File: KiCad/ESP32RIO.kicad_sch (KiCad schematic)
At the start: 40 parts, among them J1 Screw_Terminal_01x08, J2 Screw_Terminal_01x08, J3 Screw_Terminal_01x08, J4 Screw_Terminal_01x08, U1 PC817, U10 PC817, U11 PC817, U12 PC817, U13 PC817, U14 PC817, U15 DOIT-ESP32-DEVKIT-V1, U16 SP3485CN, U17 ULN2803A, U18 TB67H451FNG, U2 PC817, U3 PC817, U4 PC817, U5 PC817, U6 PC817, U7 PC817, U8 PC817, U9 PC817

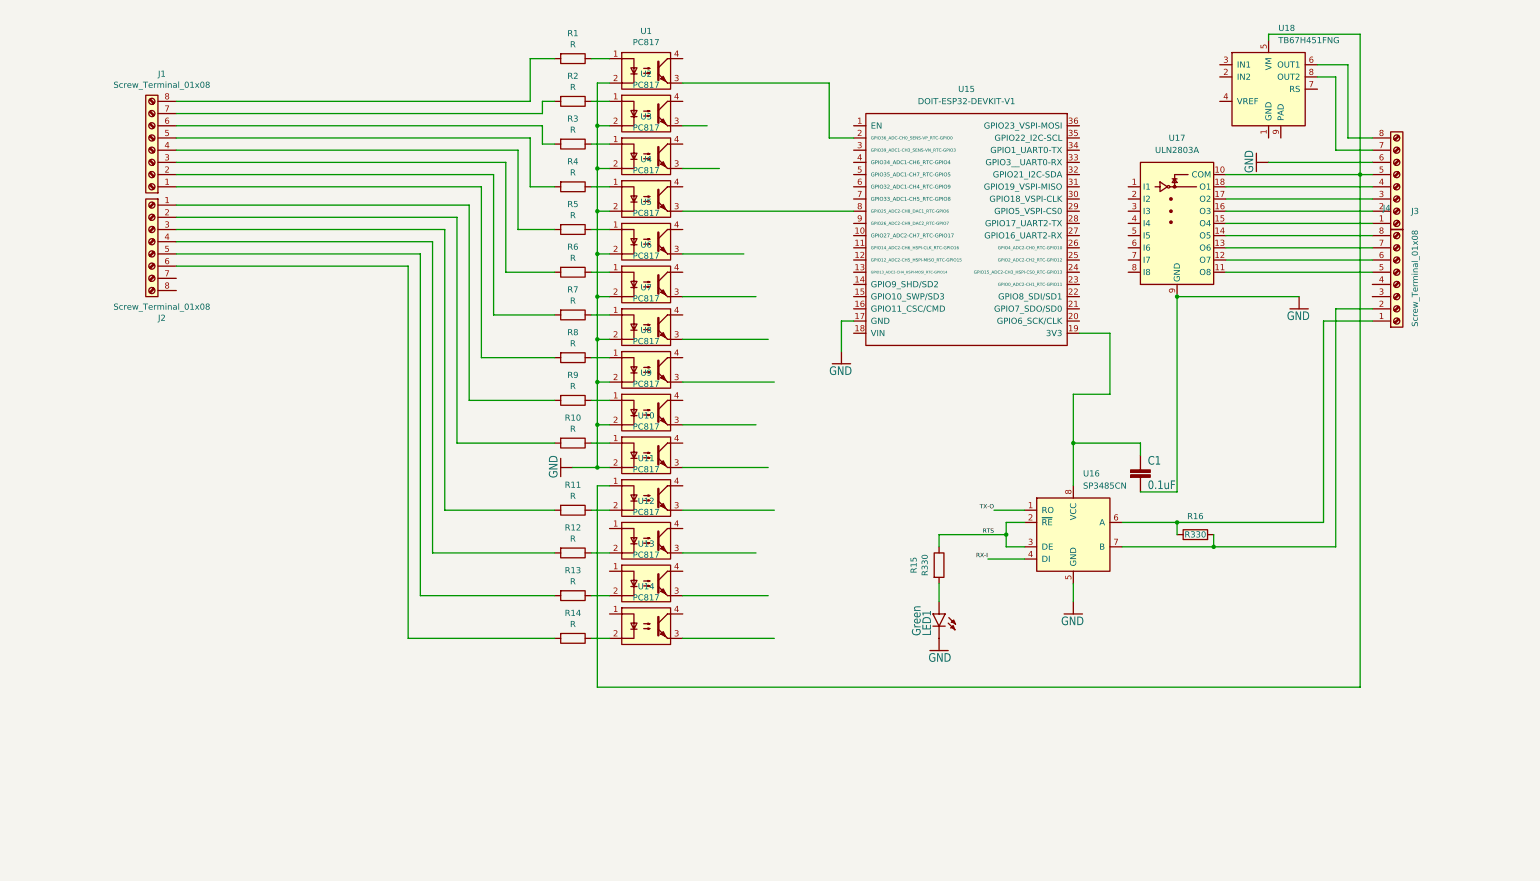
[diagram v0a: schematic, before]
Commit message: 14DI og 2 AI virker
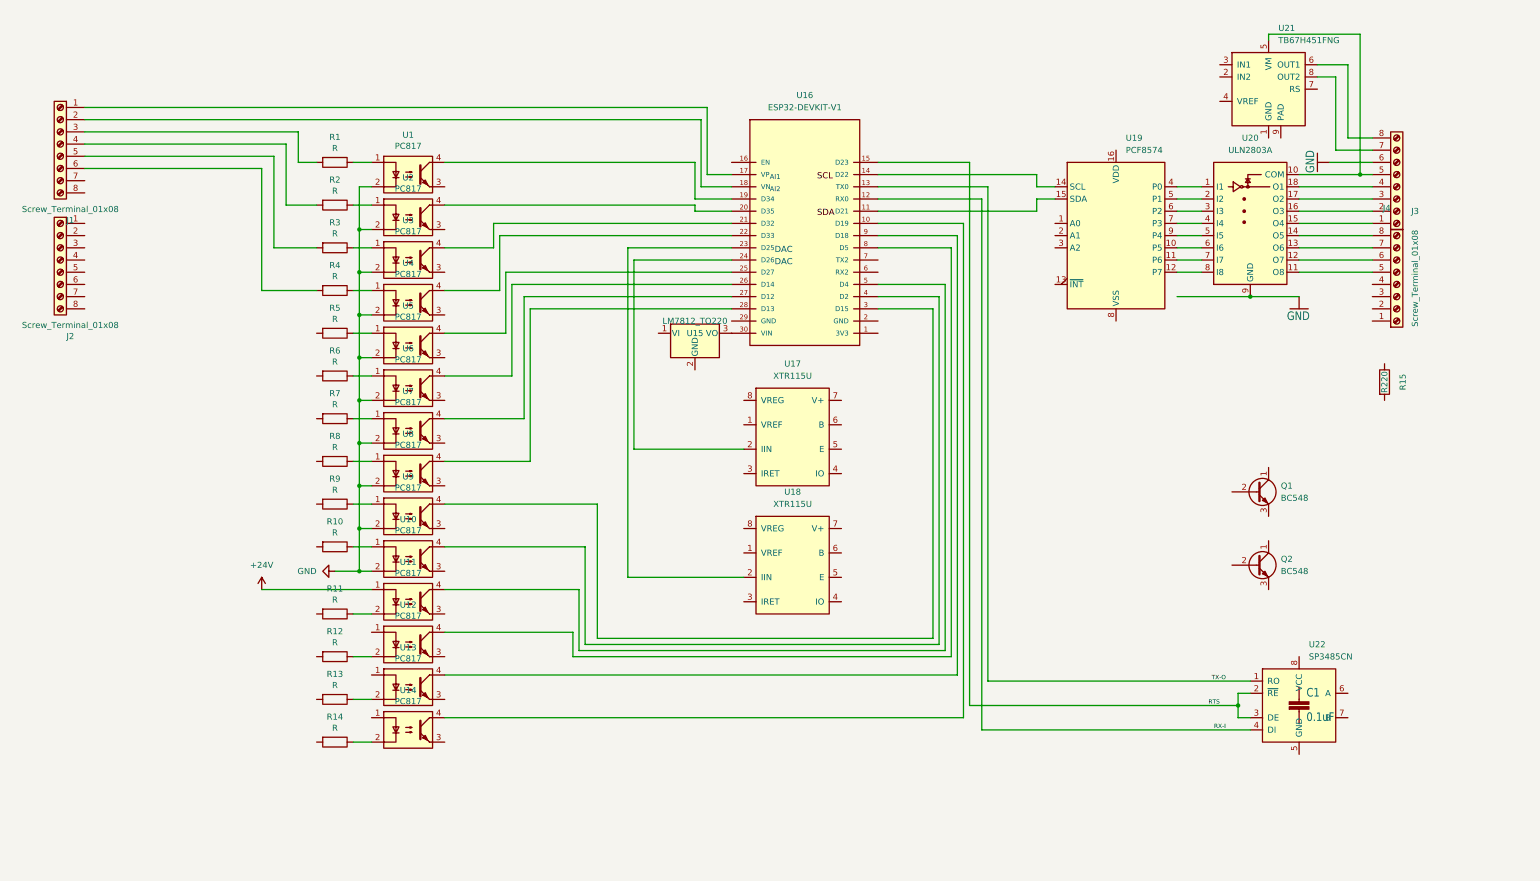
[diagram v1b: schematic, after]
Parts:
- removed LED1: Green, LED_SMD:LED_0603_1608Metric_Pad1.05x0.95mm_HandSolder, symbol RS485_Breakout-eagle-import:LED-GREEN0603
- removed R16: R330, Resistor_THT:R_Axial_DIN0204_L3.6mm_D1.6mm_P2.54mm_Vertical, symbol Device:R
- removed U15: DOIT-ESP32-DEVKIT-V1, doit-esp32-devkit-kicad:ESP32-DOIT-DEVKIT, symbol doit-esp32-devkit-v1:DOIT-ESP32-DEVKIT-V1
- added Q1, Q2: BC548, Package_TO_SOT_THT:TO-92_Inline, symbol Transistor_BJT:BC548
- added U15: LM7812_TO220, Package_TO_SOT_THT:TO-220-3_Vertical, symbol Regulator_Linear:LM7812_TO220
- added U16: ESP32-DEVKIT-V1, doit-esp32-devkit-kicad:ESP32-DOIT-DEVKIT, symbol Devkit V1-1:ESP32-DEVKIT-V1
- added U17, U18: XTR115U, Package_SO:SOIC-8_3.9x4.9mm_P1.27mm, symbol Interface_CurrentLoop:XTR115U
- added U19: PCF8574, Package_DIP:DIP-18_W7.62mm, symbol Interface_Expansion:PCF8574
- R15: value R330 -> R220
- renumbered U17 to U20, U18 to U21, U16 to U22
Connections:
- net GND: no longer C1.2, U22.5 (GND)
- net RTS: now also U16.15 (D23); no longer R15.1
- net RX-I: now also U16.12 (RX0)
- net TX-O: now also U16.13 (TX0)
- net at R4.2: now also J1.6 (Pin_6); no longer J1.5 (Pin_5)
- net at R6.2: no longer J1.3 (Pin_3)
- net at U10.4: now also U16.4 (D2)
- net at R8.2: no longer J1.1 (Pin_1)
- net at R7.2: no longer J1.2 (Pin_2)
- net at J1.4 (Pin_4): now also R2.2; no longer R5.2
- net at R3.2: now also J1.5 (Pin_5); no longer J1.6 (Pin_6)
- net at J1.7 (Pin_7): no longer R2.2
- net at R1.2: now also J1.3 (Pin_3); no longer J1.8 (Pin_8)
- net at U6.4: now also U16.26 (D14)
- net at U3.4: now also U16.21 (D32)
- net at U13.4: now also U16.9 (D18)
- net at C1.1: no longer U22.8 (VCC)
- net at R13.2: no longer J2.5 (Pin_5)
- net at R14.2: no longer J2.6 (Pin_6)
- net at J4.1 (Pin_1): no longer U22.6 (A)
- net at J4.2 (Pin_2): no longer U22.7 (B)
- net at R9.2: no longer J2.1 (Pin_1)
- net at U7.4: now also U16.27 (D12)
- net at J3.5 (Pin_5), U20.10 (COM), U21.5 (VM): no longer U11.1
- net at R10.2: no longer J2.2 (Pin_2)
- net at R11.2: no longer J2.3 (Pin_3)
- net at R12.2: no longer J2.4 (Pin_4)
- net at U12.4: now also U16.8 (D5)
- net at U4.4: now also U16.22 (D33)
- net at U1.4: now also U16.19 (D34)
- net at U11.4: now also U16.5 (D4)
- net at U2.4: now also U16.20 (D35)
- net at U20.1 (I1): now also U19.4 (P0)
- net at U20.2 (I2): now also U19.5 (P1)
- net at U20.3 (I3): now also U19.6 (P2)
- net at U20.4 (I4): now also U19.7 (P3)
- net at U20.5 (I5): now also U19.9 (P4)
- net at U20.6 (I6): now also U19.10 (P5)
- net at U20.7 (I7): now also U19.11 (P6)
- net at U20.8 (I8): now also U19.12 (P7)
- net at U14.4: now also U16.10 (D19)
- net at U9.4: now also U16.3 (D15)
- net at U8.4: now also U16.28 (D13)
- net at U5.4: now also U16.25 (D27)
- new net: U16.14 (D22), U19.14 (SCL)
- new net: U16.11 (D21), U19.15 (SDA)
- new net: U16.23 (D25), U18.2 (IIN)
- new net: U15.3 (VO), U16.30 (VIN)
- new net: U16.24 (D26), U17.2 (IIN)
- new net: J1.1 (Pin_1), U16.17 (VP)
- new net: J1.2 (Pin_2), U16.18 (VN)
- new net +24V: U11.1
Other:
- note added: "AI1"
- note added: "AI2"
- note added: "DAC"
- moved on the sheet: C1, R1, R10, R11, R12, R13, R14, R2, R3, R4, R5, R6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

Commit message: Lagt til utganger og funnet problemer med 4-20mA ut
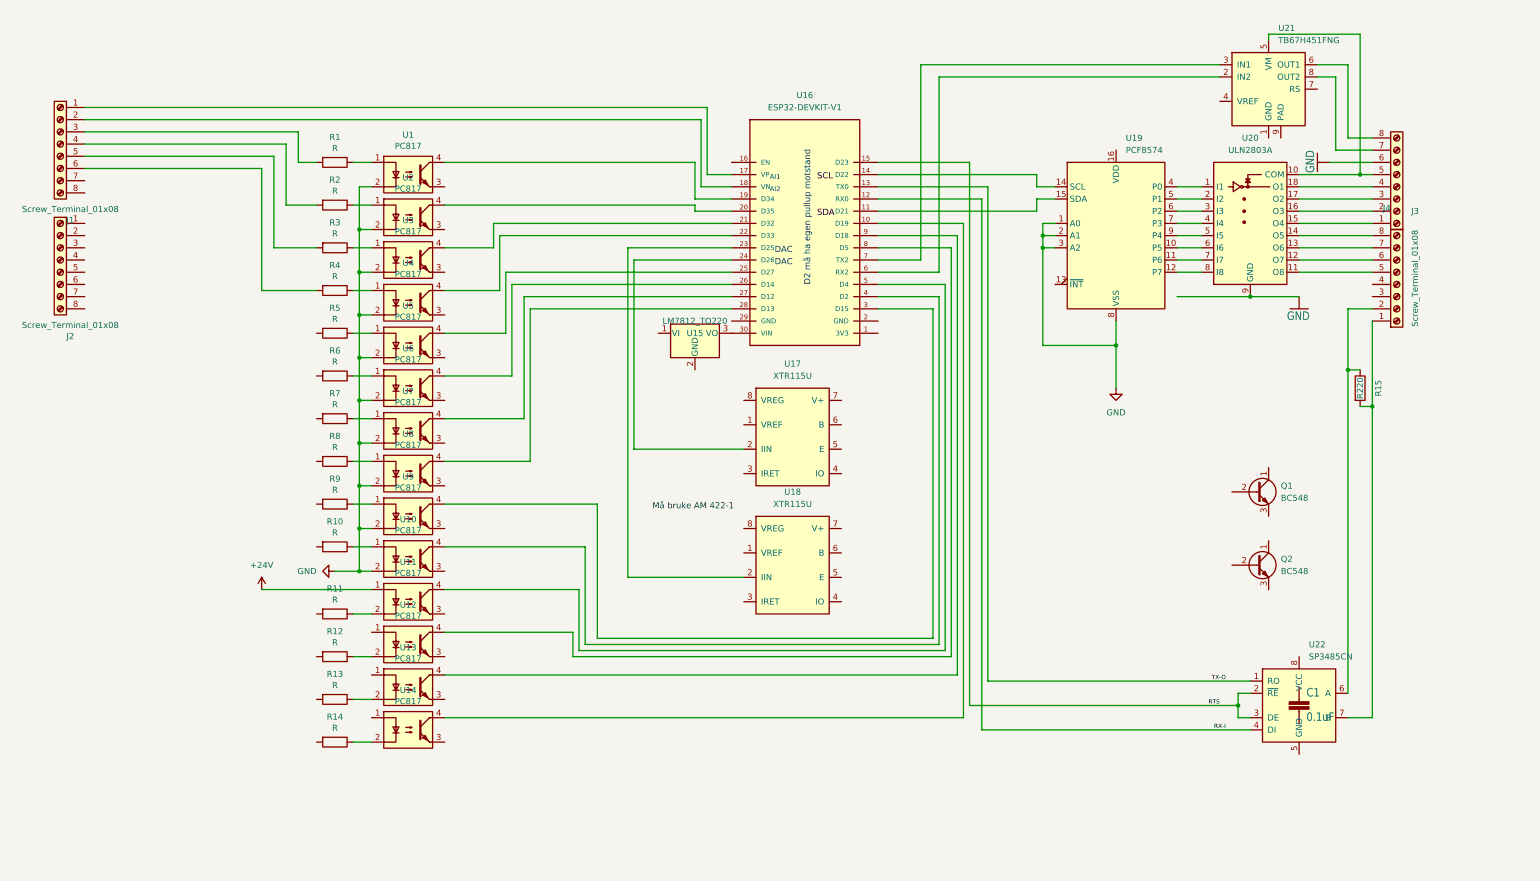
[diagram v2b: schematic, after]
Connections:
- net GND: now also U19.1 (A0), U19.2 (A1), U19.3 (A2), U19.8 (VSS)
- net at R15.1: now also J4.2 (Pin_2), U22.6 (A)
- net at R15.2: now also J4.1 (Pin_1), U22.7 (B)
- net at U21.2 (IN2): now also U16.6 (RX2)
- net at U21.3 (IN1): now also U16.7 (TX2)
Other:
- note added: "D2 må ha egen pullup motstand"
- note added: "Må bruke AM 422-1"
- moved on the sheet: R15
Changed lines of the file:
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@@
   (junction (at 64.77 99.06) (diameter 0) (color 0 0 0 0)
   )
+  (junction (at 222.25 78.74) (diameter 0) (color 0 0 0 0)
+  )
+  (junction (at 275.59 91.44) (diameter 0) (color 0 0 0 0)
+  )
+  (junction (at 207.01 58.42) (diameter 0) (color 0 0 0 0)
+  )
   (junction (at 64.77 90.17) (diameter 0) (color 0 0 0 0)
   )
   (junction (at 250.19 68.58) (diameter 0) (color 0 0 0 0)
   )
+  (junction (at 207.01 55.88) (diameter 0) (color 0 0 0 0)
+  )
   (junction (at 64.77 72.39) (diameter 0) (color 0 0 0 0)
   )
+  (junction (at 270.51 83.82) (diameter 0) (color 0 0 0 0)
+  )
   (junction (at 273.05 43.18) (diameter 0) (color 0 0 0 0)
   )
@@
     (stroke (width 0) (type default) (color 0 0 0 0))
   )
+  (wire (pts (xy 185.42 22.86) (xy 243.84 22.86))
+    (stroke (width 0) (type default) (color 0 0 0 0))
+  )
   (wire (pts (xy 82.55 67.31) (xy 93.98 67.31))
     (stroke (width 0) (type default) (color 0 0 0 0))
@@
     (stroke (width 0) (type default) (color 0 0 0 0))
   )
+  (wire (pts (xy 207.01 53.34) (xy 207.01 55.88))
+    (stroke (width 0) (type default) (color 0 0 0 0))
+  )
   (wire (pts (xy 64.77 107.95) (xy 67.31 107.95))
     (stroke (width 0) (type default) (color 0 0 0 0))
@@
     (stroke (width 0) (type default) (color 0 0 0 0))
   )
+  (wire (pts (xy 270.51 151.13) (xy 270.51 83.82))
+    (stroke (width 0) (type default) (color 0 0 0 0))
+  )
+  (wire (pts (xy 172.72 63.5) (xy 185.42 63.5))
+    (stroke (width 0) (type default) (color 0 0 0 0))
+  )
   (wire (pts (xy 7.62 41.91) (xy 44.45 41.91))
     (stroke (width 0) (type default) (color 0 0 0 0))
   )
+  (wire (pts (xy 207.01 58.42) (xy 207.01 78.74))
+    (stroke (width 0) (type default) (color 0 0 0 0))
+  )
   (wire (pts (xy 260.35 50.8) (xy 275.59 50.8))
     (stroke (width 0) (type default) (color 0 0 0 0))
   )
+  (wire (pts (xy 209.55 53.34) (xy 207.01 53.34))
+    (stroke (width 0) (type default) (color 0 0 0 0))
+  )
   (wire (pts (xy 109.22 143.51) (xy 187.96 143.51))
     (stroke (width 0) (type default) (color 0 0 0 0))
   )
+  (wire (pts (xy 270.51 71.12) (xy 275.59 71.12))
+    (stroke (width 0) (type default) (color 0 0 0 0))
+  )
   (wire (pts (xy 82.55 129.54) (xy 110.49 129.54))
     (stroke (width 0) (type default) (color 0 0 0 0))
@@
     (stroke (width 0) (type default) (color 0 0 0 0))
   )
+  (wire (pts (xy 207.01 55.88) (xy 209.55 55.88))
+    (stroke (width 0) (type default) (color 0 0 0 0))
+  )
   (wire (pts (xy 64.77 107.95) (xy 64.77 116.84))
     (stroke (width 0) (type default) (color 0 0 0 0))
@@
     (stroke (width 0) (type default) (color 0 0 0 0))
   )
+  (wire (pts (xy 172.72 60.96) (xy 181.61 60.96))
+    (stroke (width 0) (type default) (color 0 0 0 0))
+  )
   (wire (pts (xy 121.92 60.96) (xy 142.24 60.96))
     (stroke (width 0) (type default) (color 0 0 0 0))
@@
     (stroke (width 0) (type default) (color 0 0 0 0))
   )
+  (wire (pts (xy 207.01 58.42) (xy 207.01 55.88))
+    (stroke (width 0) (type default) (color 0 0 0 0))
+  )
   (wire (pts (xy 273.05 43.18) (xy 275.59 43.18))
     (stroke (width 0) (type default) (color 0 0 0 0))
@@
     (stroke (width 0) (type default) (color 0 0 0 0))
   )
+  (wire (pts (xy 209.55 58.42) (xy 207.01 58.42))
+    (stroke (width 0) (type default) (color 0 0 0 0))
+  )
+  (wire (pts (xy 222.25 73.66) (xy 222.25 78.74))
+    (stroke (width 0) (type default) (color 0 0 0 0))
+  )
   (wire (pts (xy 184.15 71.12) (xy 172.72 71.12))
     (stroke (width 0) (type default) (color 0 0 0 0))
@@
     (stroke (width 0) (type default) (color 0 0 0 0))
   )
+  (wire (pts (xy 270.51 83.82) (xy 270.51 71.12))
+    (stroke (width 0) (type default) (color 0 0 0 0))
+  )
   (wire (pts (xy 234.95 63.5) (xy 240.03 63.5))
     (stroke (width 0) (type default) (color 0 0 0 0))
@@
     (stroke (width 0) (type default) (color 0 0 0 0))
   )
+  (wire (pts (xy 270.51 83.82) (xy 273.05 83.82))
+    (stroke (width 0) (type default) (color 0 0 0 0))
+  )
+  (wire (pts (xy 275.59 73.66) (xy 275.59 91.44))
+    (stroke (width 0) (type default) (color 0 0 0 0))
+  )
+  (wire (pts (xy 270.51 156.21) (xy 275.59 156.21))
+    (stroke (width 0) (type default) (color 0 0 0 0))
+  )
   (wire (pts (xy 99.06 68.58) (xy 142.24 68.58))
     (stroke (width 0) (type default) (color 0 0 0 0))
@@
     (stroke (width 0) (type default) (color 0 0 0 0))
   )
+  (wire (pts (xy 222.25 78.74) (xy 222.25 87.63))
+    (stroke (width 0) (type default) (color 0 0 0 0))
+  )
   (wire (pts (xy 63.5 102.87) (xy 67.31 102.87))
     (stroke (width 0) (type default) (color 0 0 0 0))
@@
     (stroke (width 0) (type default) (color 0 0 0 0))
   )
+  (wire (pts (xy 181.61 60.96) (xy 181.61 20.32))
+    (stroke (width 0) (type default) (color 0 0 0 0))
+  )
   (wire (pts (xy 64.77 81.28) (xy 67.31 81.28))
     (stroke (width 0) (type default) (color 0 0 0 0))
@@
     (stroke (width 0) (type default) (color 0 0 0 0))
   )
+  (wire (pts (xy 273.05 91.44) (xy 275.59 91.44))
+    (stroke (width 0) (type default) (color 0 0 0 0))
+  )
   (wire (pts (xy 82.55 93.98) (xy 99.06 93.98))
     (stroke (width 0) (type default) (color 0 0 0 0))
@@
     (stroke (width 0) (type default) (color 0 0 0 0))
   )
+  (wire (pts (xy 181.61 20.32) (xy 243.84 20.32))
+    (stroke (width 0) (type default) (color 0 0 0 0))
+  )
   (wire (pts (xy 63.5 76.2) (xy 67.31 76.2))
     (stroke (width 0) (type default) (color 0 0 0 0))
@@
     (stroke (width 0) (type default) (color 0 0 0 0))
   )
+  (wire (pts (xy 185.42 63.5) (xy 185.42 22.86))
+    (stroke (width 0) (type default) (color 0 0 0 0))
+  )
   (wire (pts (xy 247.65 153.67) (xy 247.65 156.21))
     (stroke (width 0) (type default) (color 0 0 0 0))
@@
     (stroke (width 0) (type default) (color 0 0 0 0))
   )
+  (wire (pts (xy 222.25 78.74) (xy 207.01 78.74))
+    (stroke (width 0) (type default) (color 0 0 0 0))
+  )
   (wire (pts (xy 234.95 68.58) (xy 250.19 68.58))
     (stroke (width 0) (type default) (color 0 0 0 0))
@@
   )
   (wire (pts (xy 109.22 138.43) (xy 109.22 143.51))
+    (stroke (width 0) (type default) (color 0 0 0 0))
+  )
+  (wire (pts (xy 275.59 91.44) (xy 275.59 156.21))
     (stroke (width 0) (type default) (color 0 0 0 0))
   )
@@
     (effects (font (size 1.27 1.27)) (justify right bottom))
   )
+  (text "Må bruke AM 422-1" (at 125.73 113.03 0)
+    (effects (font (size 1.27 1.27)) (justify left bottom))
+  )
   (text "AI2" (at 152.4 46.99 180)
     (effects (font (size 1 1)) (justify right bottom))
@@
   (text "AI1" (at 152.4 44.45 180)
     (effects (font (size 1 1)) (justify right bottom))
+  )
+  (text "D2 må ha egen pullup motstand" (at 158.75 38.1 270)
+    (effects (font (size 1.27 1.27)) (justify right bottom))
   )
   (label "SDA" (at 160.02 52.07 0)
@@
     (pin "1")
     (pin "2")
+  )
+  (symbol (lib_id "power:GND") (at 222.25 87.63 0) (unit 1)
+    (in_bom yes) (on_board yes) (fields_autoplaced)
+    (property "Reference" "#PWR?" (id 0) (at 222.25 93.98 0)
+      (effects (font (size 1.27 1.27)) hide)
+    )
+    (property "Value" "GND" (id 1) (at 222.25 92.71 0))
+    (property "Footprint" "" (id 2) (at 222.25 87.63 0)
+      (effects (font (size 1.27 1.27)) hide)
+    )
+    (property "Datasheet" "" (id 3) (at 222.25 87.63 0)
+      (effects (font (size 1.27 1.27)) hide)
+    )
+    (pin "1")
   )
   (symbol (lib_id "Interface_Expansion:PCF8574") (at 222.25 55.88 0) (unit 1)
@@
     (pin "1")
   )
-  (symbol (lib_id "Device:R") (at 278.13 86.36 0) (unit 1)
-    (in_bom yes) (on_board yes)
-    (property "Reference" "R15" (id 0) (at 281.94 86.36 90))
-    (property "Value" "R220" (id 1) (at 278.13 86.36 90))
-    (property "Footprint" "Resistor_THT:R_Axial_DIN0204_L3.6mm_D1.6mm_P2.54mm_Vertical" (id 2) (at 276.352 86.36 90)
-      (effects (font (size 1.27 1.27)) hide)
-    )
-    (property "Datasheet" "~" (id 3) (at 278.13 86.36 0)
+  (symbol (lib_id "Device:R") (at 273.05 87.63 0) (unit 1)
+    (in_bom yes) (on_board yes)
+    (property "Reference" "R15" (id 0) (at 276.86 87.63 90))
+    (property "Value" "R220" (id 1) (at 273.05 87.63 90))
+    (property "Footprint" "Resistor_THT:R_Axial_DIN0204_L3.6mm_D1.6mm_P2.54mm_Vertical" (id 2) (at 271.272 87.63 90)
+      (effects (font (size 1.27 1.27)) hide)
+    )
+    (property "Datasheet" "~" (id 3) (at 273.05 87.63 0)
       (effects (font (size 1.27 1.27)) hide)
     )
@@
       (reference "#PWR01") (unit 1) (value "+24V") (footprint "")
     )
+    (path "/0bfaa4de-3935-41ae-8049-0c49bc60ead6"
+      (reference "#PWR?") (unit 1) (value "GND") (footprint "")
+    )
     (path "/207aa811-dd6d-483c-a649-1de1ea04630d"
